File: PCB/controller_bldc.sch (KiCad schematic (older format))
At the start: 72 parts, among them J1 Battery Supply, J2 Conn_01x11_Male, J6 LM35, J7 Hall Sensors, J9 BLDC Motor, K1 RAYEX-L90B, Q1 IRF1010N, Q2 IRF1010N, Q3 IRF1010N, Q4 IRF1010N, Q5 IRF1010N, Q6 IRF1010N, Q7 PN2222A, U1 ESP32-DEVKITC-32D, U2 Opamp_Dual_Generic, U3 LM2596SOURCE_Pin2, U4 IR2103, U5 LM2596SOURCE, U8 IR2103, U9 IR2103

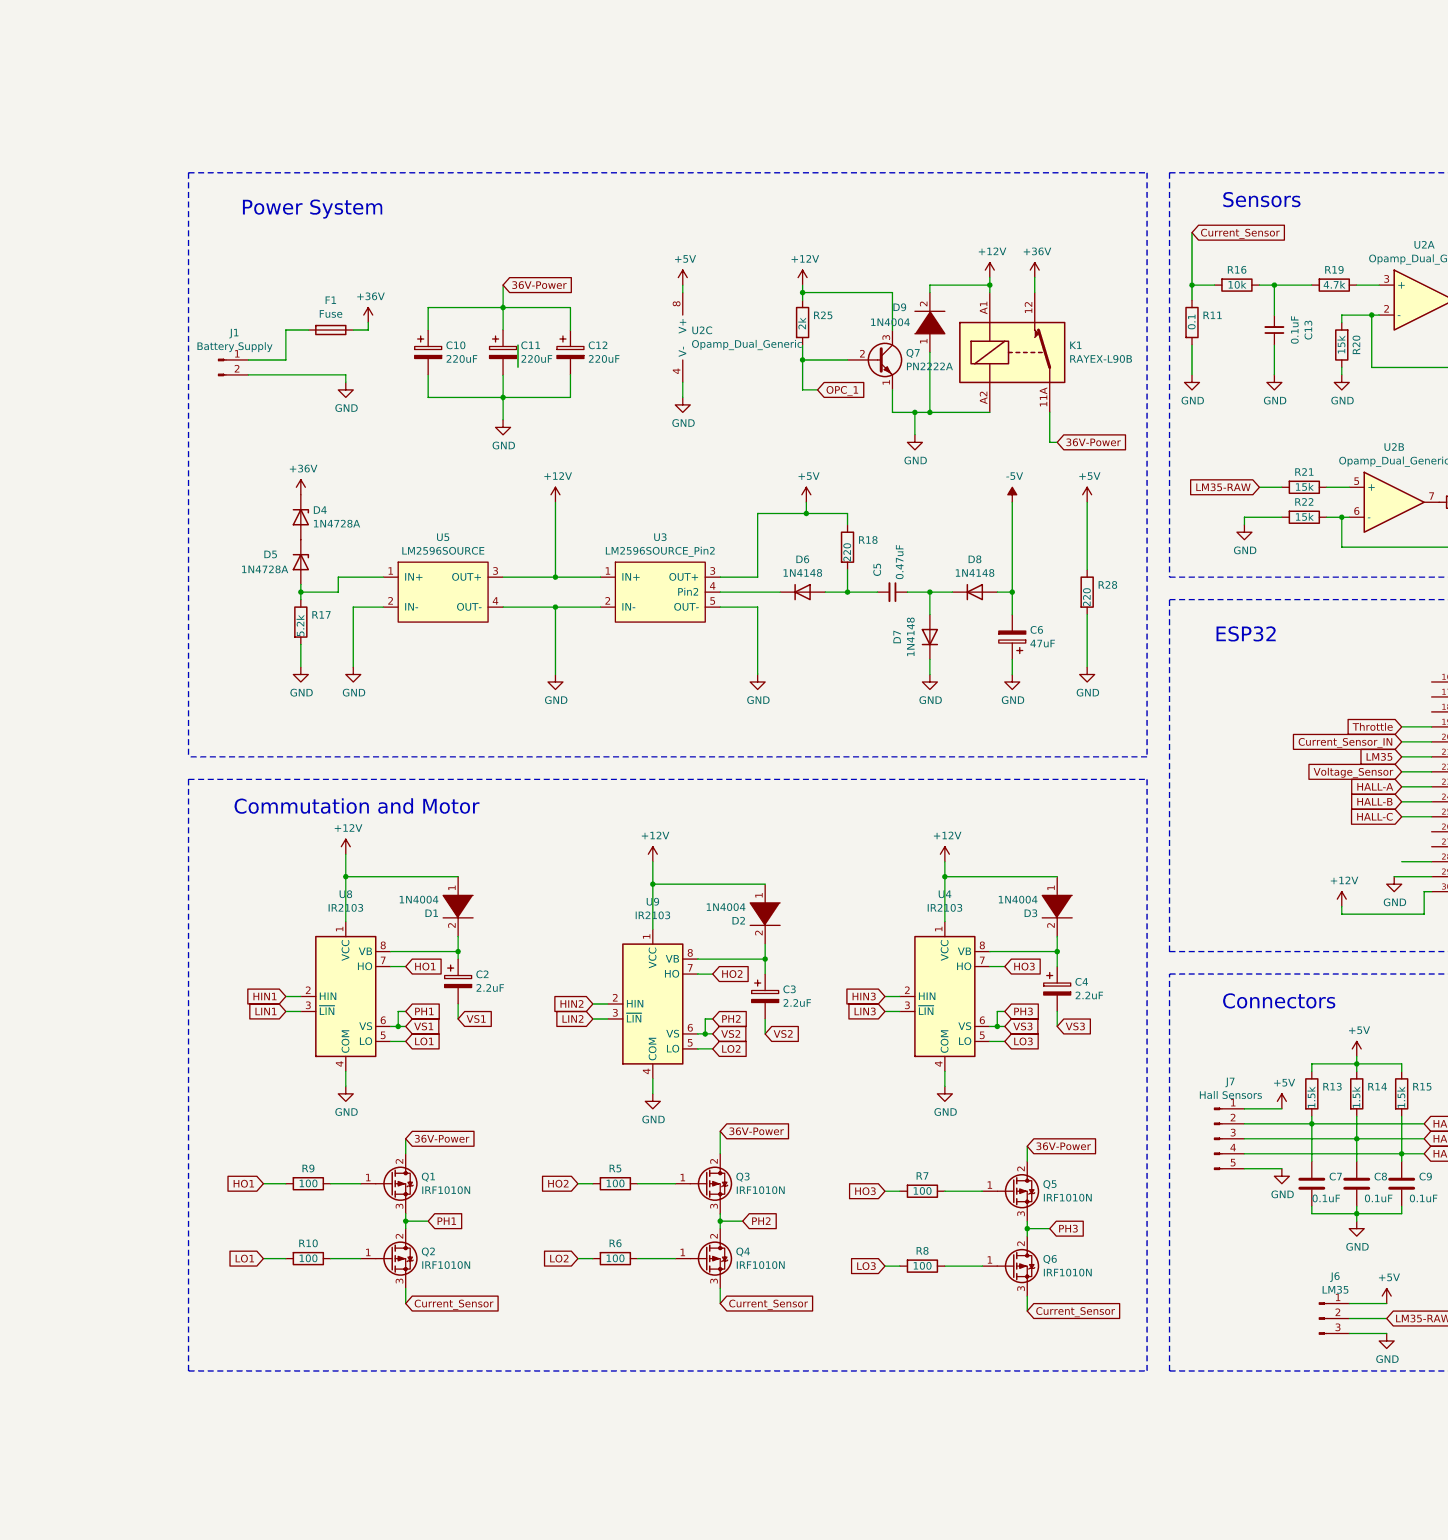
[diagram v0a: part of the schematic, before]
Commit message: Changing all the schematics
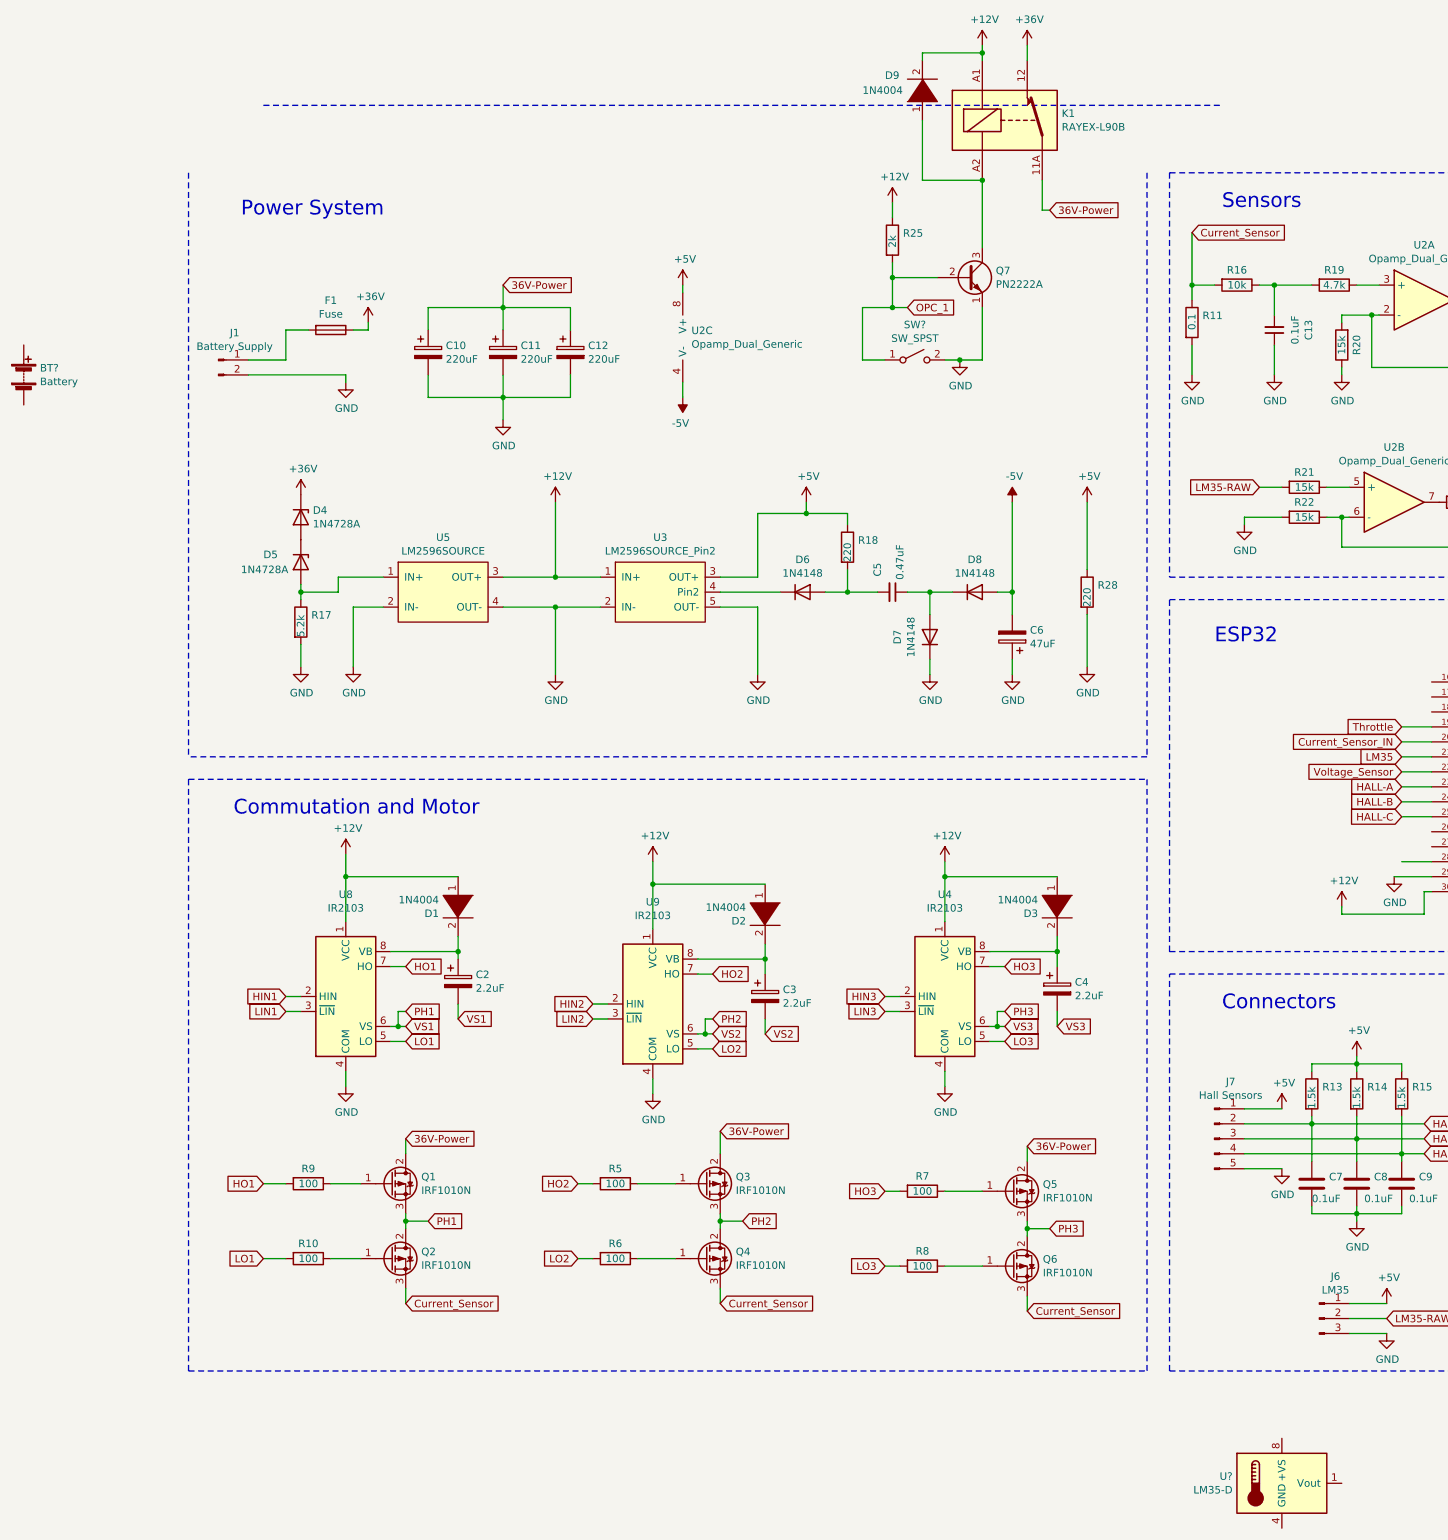
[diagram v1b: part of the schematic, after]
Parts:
- added BT?: Battery, symbol Device:Battery
- added SW?: SW_SPST, symbol Switch:SW_SPST
- added U?: LM35-D, Package_SO:SOIC-8_3.9x4.9mm_P1.27mm, symbol Sensor_Temperature:LM35-D
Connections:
- net +12V: no longer Q7.3 (C)
- net -5V: now also U2.4 (V-)
- net GND: now also SW?.2 (B); no longer D9.1 (K), K1.A2, U2.4 (V-)
- net OPC_1: now also SW?.1 (A)
- new net: D9.1 (K), K1.A2, Q7.3 (C)
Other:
- moved on the sheet: D9, K1, Q7, R25
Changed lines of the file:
@@
 	2700 1050 2250 1050
-Wire Wire Line
-	2350 1450 2350 1300
 Wire Wire Line
 	2250 1050 2250 1200
@@
 $EndComp
 Wire Wire Line
-	4250 1400 4550 1400
-Wire Wire Line
-	4250 1600 4250 1400
-Wire Wire Line
-	4350 1600 4250 1600
-Text GLabel 4350 1600 2    50   Input ~ 0
+	4850 850  5150 850
+Wire Wire Line
+	4850 1050 4850 850
+Wire Wire Line
+	4950 1050 4850 1050
+Text GLabel 4950 1050 2    50   Input ~ 0
 OPC_1
-Wire Wire Line
-	5000 1750 5100 1750
-Connection ~ 5000 1750
-Wire Wire Line
-	5000 1900 5000 1750
-Connection ~ 5100 1750
-Wire Wire Line
-	4850 1750 5000 1750
 $Comp
 L power:GND #PWR0109
 U 1 1 618C8BBA
-P 5000 1900
-F 0 "#PWR0109" H 5000 1650 50  0001 C CNN
-F 1 "GND" H 5005 1727 50  0000 C CNN
-F 2 "" H 5000 1900 50  0001 C CNN
-F 3 "" H 5000 1900 50  0001 C CNN
-	1    5000 1900
-	1    0    0    -1
-$EndComp
-Wire Wire Line
-	4850 1600 4850 1750
-Wire Wire Line
-	5100 1750 5500 1750
-Wire Wire Line
-	5100 1350 5100 1750
-Wire Wire Line
-	5500 900  5500 950
-Connection ~ 5500 900
-Wire Wire Line
-	5100 900  5500 900
-Wire Wire Line
-	5100 950  5100 900
-Wire Wire Line
-	4250 950  4850 950
-Wire Wire Line
-	4850 1200 4850 950
-Wire Wire Line
-	5500 850  5500 900
-Connection ~ 4250 950
-Wire Wire Line
-	4250 950  4250 1000
-Wire Wire Line
-	4250 900  4250 950
+P 5300 1400
+F 0 "#PWR0109" H 5300 1150 50  0001 C CNN
+F 1 "GND" H 5305 1227 50  0000 C CNN
+F 2 "" H 5300 1400 50  0001 C CNN
+F 3 "" H 5300 1400 50  0001 C CNN
+	1    5300 1400
+	1    0    0    -1
+$EndComp
+Wire Wire Line
+	5050 200  5450 200
+Wire Wire Line
+	5050 -200 5050 200
+Wire Wire Line
+	5450 -650 5450 -600
+Connection ~ 5450 -650
+Wire Wire Line
+	5050 -650 5450 -650
+Wire Wire Line
+	5050 -600 5050 -650
+Wire Wire Line
+	5450 -700 5450 -650
 $Comp
 L pspice:DIODE D9
 U 1 1 6101C203
-P 5100 1150
-F 0 "D9" V 5200 1400 50  0000 R CNN
-F 1 "1N4004" V 5100 1550 50  0000 R CNN
-F 2 "Diode_THT:D_DO-35_SOD27_P7.62mm_Horizontal" H 5100 1150 50  0001 C CNN
-F 3 "~" H 5100 1150 50  0001 C CNN
-	1    5100 1150
+P 5050 -400
+F 0 "D9" V 5150 -150 50  0000 R CNN
+F 1 "1N4004" V 5050 0   50  0000 R CNN
+F 2 "Diode_THT:D_DO-35_SOD27_P7.62mm_Horizontal" H 5050 -400 50  0001 C CNN
+F 3 "~" H 5050 -400 50  0001 C CNN
+	1    5050 -400
 	0    -1   -1   0
 $EndComp
 Wire Wire Line
-	5800 850  5800 950
+	5750 -700 5750 -600
 $Comp
 L Relay:RAYEX-L90B K1
 U 1 1 6114BA59
-P 5700 1350
-F 0 "K1" H 6030 1396 50  0000 L CNN
-F 1 "RAYEX-L90B" H 6030 1305 50  0000 L CNN
-F 2 "Relay_THT:Relay_SPST_RAYEX-L90B" H 6050 1300 50  0001 L CNN
-F 3 "https://a3.sofastcdn.com/attachment/7jioKBjnRiiSrjrjknRiwS77gwbf3zmp/L90-SERIES.pdf" H 6200 1200 50  0001 L CNN
-	1    5700 1350
+P 5650 -200
+F 0 "K1" H 5980 -154 50  0000 L CNN
+F 1 "RAYEX-L90B" H 5980 -245 50  0000 L CNN
+F 2 "Relay_THT:Relay_SPST_RAYEX-L90B" H 6000 -250 50  0001 L CNN
+F 3 "https://a3.sofastcdn.com/attachment/7jioKBjnRiiSrjrjknRiwS77gwbf3zmp/L90-SERIES.pdf" H 6150 -350 50  0001 L CNN
+	1    5650 -200
 	1    0    0    -1
 $EndComp
@@
 L Device:R R25
 U 1 1 61021042
-P 4250 1150
-F 0 "R25" H 4320 1196 50  0000 L CNN
-F 1 "2k" V 4250 1100 50  0000 L CNN
-F 2 "Resistor_THT:R_Axial_DIN0207_L6.3mm_D2.5mm_P10.16mm_Horizontal" V 4180 1150 50  0001 C CNN
-F 3 "~" H 4250 1150 50  0001 C CNN
-	1    4250 1150
+P 4850 600
+F 0 "R25" H 4920 646 50  0000 L CNN
+F 1 "2k" V 4850 550 50  0000 L CNN
+F 2 "Resistor_THT:R_Axial_DIN0207_L6.3mm_D2.5mm_P10.16mm_Horizontal" V 4780 600 50  0001 C CNN
+F 3 "~" H 4850 600 50  0001 C CNN
+	1    4850 600
 	1    0    0    -1
 $EndComp
@@
 L Transistor_BJT:PN2222A Q7
 U 1 1 6101E23D
-P 4750 1400
-F 0 "Q7" H 4940 1446 50  0000 L CNN
-F 1 "PN2222A" H 4940 1355 50  0000 L CNN
-F 2 "Package_TO_SOT_THT:TO-92_Inline" H 4950 1325 50  0001 L CIN
-F 3 "https://www.onsemi.com/pub/Collateral/PN2222-D.PDF" H 4750 1400 50  0001 L CNN
-	1    4750 1400
-	1    0    0    -1
-$EndComp
-Connection ~ 4250 1400
-Wire Wire Line
-	4250 1300 4250 1400
+P 5350 850
+F 0 "Q7" H 5540 896 50  0000 L CNN
+F 1 "PN2222A" H 5540 805 50  0000 L CNN
+F 2 "Package_TO_SOT_THT:TO-92_Inline" H 5550 775 50  0001 L CIN
+F 3 "https://www.onsemi.com/pub/Collateral/PN2222-D.PDF" H 5350 850 50  0001 L CNN
+	1    5350 850
+	1    0    0    -1
+$EndComp
+Connection ~ 4850 850
+Wire Wire Line
+	4850 750  4850 850
 $Comp
 L power:+12V #PWR0134
 U 1 1 6106A128
-P 5500 850
-F 0 "#PWR0134" H 5500 700 50  0001 C CNN
-F 1 "+12V" H 5515 1023 50  0000 C CNN
-F 2 "" H 5500 850 50  0001 C CNN
-F 3 "" H 5500 850 50  0001 C CNN
-	1    5500 850
-	1    0    0    -1
-$EndComp
-Wire Wire Line
-	5900 1750 5900 1950
+P 5450 -700
+F 0 "#PWR0134" H 5450 -850 50  0001 C CNN
+F 1 "+12V" H 5465 -527 50  0000 C CNN
+F 2 "" H 5450 -700 50  0001 C CNN
+F 3 "" H 5450 -700 50  0001 C CNN
+	1    5450 -700
+	1    0    0    -1
+$EndComp
+Wire Wire Line
+	5850 200  5850 400
 $Comp
 L power:+36V #PWR03
 U 1 1 607E0827
-P 5800 850
-F 0 "#PWR03" H 5800 700 50  0001 C CNN
-F 1 "+36V" H 5815 1023 50  0000 C CNN
-F 2 "" H 5800 850 50  0001 C CNN
-F 3 "" H 5800 850 50  0001 C CNN
-	1    5800 850
+P 5750 -700
+F 0 "#PWR03" H 5750 -850 50  0001 C CNN
+F 1 "+36V" H 5765 -527 50  0000 C CNN
+F 2 "" H 5750 -700 50  0001 C CNN
+F 3 "" H 5750 -700 50  0001 C CNN
+	1    5750 -700
 	1    0    0    -1
 $EndComp
@@
 L power:+12V #PWR0110
 U 1 1 60E85274
-P 4250 900
-F 0 "#PWR0110" H 4250 750 50  0001 C CNN
-F 1 "+12V" H 4265 1073 50  0000 C CNN
-F 2 "" H 4250 900 50  0001 C CNN
-F 3 "" H 4250 900 50  0001 C CNN
-	1    4250 900
-	1    0    0    -1
-$EndComp
-Wire Wire Line
-	5900 1950 5950 1950
-Text GLabel 5950 1950 2    50   Input ~ 0
+P 4850 350
+F 0 "#PWR0110" H 4850 200 50  0001 C CNN
+F 1 "+12V" H 4865 523 50  0000 C CNN
+F 2 "" H 4850 350 50  0001 C CNN
+F 3 "" H 4850 350 50  0001 C CNN
+	1    4850 350
+	1    0    0    -1
+$EndComp
+Wire Wire Line
+	5850 400  5900 400
+Text GLabel 5900 400  2    50   Input ~ 0
 36V-Power
 $Comp
@@
 Wire Wire Line
 	3450 1550 3450 1650
-$Comp
-L power:GND #PWR0131
-U 1 1 60CCCE5C
-P 3450 1650
-F 0 "#PWR0131" H 3450 1400 50  0001 C CNN
-F 1 "GND" H 3455 1477 50  0000 C CNN
-F 2 "" H 3450 1650 50  0001 C CNN
-F 3 "" H 3450 1650 50  0001 C CNN
-	1    3450 1650
-	1    0    0    -1
-$EndComp
 $Comp
 L power:+5V #PWR0130
@@
 LM35
 Wire Notes Line
-	150  150  6550 150
+	650  -300 7050 -300
 Wire Wire Line
 	800  1200 800  1400
@@
 Wire Wire Line
 	6150 2800 6150 2350
+$Comp
+L power:-5V #PWR0127
+U 1 1 609F2616
+P 3450 1650
+F 0 "#PWR0127" H 3450 1750 50  0001 C CNN
+F 1 "-5V" H 3465 1823 50  0000 C CNN
+F 2 "" H 3450 1650 50  0001 C CNN
+F 3 "" H 3450 1650 50  0001 C CNN
+	1    3450 1650
+	-1   0    0    1
+$EndComp
+$Comp
+L Switch:SW_SPST SW?
+U 1 1 60A2738A
+P 5000 1400
+F 0 "SW?" H 5000 1635 50  0000 C CNN
+F 1 "SW_SPST" H 5000 1544 50  0000 C CNN
+F 2 "" H 5000 1400 50  0001 C CNN
+F 3 "~" H 5000 1400 50  0001 C CNN
+	1    5000 1400
+	1    0    0    -1
+$EndComp
+Wire Wire Line
+	4800 1400 4650 1400
+Wire Wire Line
+	4650 1400 4650 1050
+Wire Wire Line
+	4650 1050 4850 1050
+Connection ~ 4850 1050
+Wire Wire Line
+	5200 1400 5300 1400
+$Comp
+L Device:Battery BT?
+U 1 1 60A5358C
+P -950 1500
+F 0 "BT?" H -842 1546 50  0000 L CNN
+F 1 "Battery" H -842 1455 50  0000 L CNN
+F 2 "" V -950 1560 50  0001 C CNN
+F 3 "~" V -950 1560 50  0001 C CNN
+	1    -950 1500
+	1    0    0    -1
+$EndComp
+$Comp
+L Sensor_Temperature:LM35-D U?
+U 1 1 60A5764A
+P 7450 8900
+F 0 "U?" H 7121 8946 50  0000 R CNN
+F 1 "LM35-D" H 7121 8855 50  0000 R CNN
+F 2 "Package_SO:SOIC-8_3.9x4.9mm_P1.27mm" H 7450 8500 50  0001 C CNN
+F 3 "http://www.ti.com/lit/ds/symlink/lm35.pdf" H 7450 8900 50  0001 C CNN
+	1    7450 8900
+	1    0    0    -1
+$EndComp
+Wire Wire Line
+	5450 1050 5450 1400
+Wire Wire Line
+	4850 350  4850 450
+Connection ~ 5300 1400
+Wire Wire Line
+	5300 1400 5450 1400
+Wire Wire Line
+	5450 200  5450 650
+Connection ~ 5450 200
 $EndSCHEMATC

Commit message: Just before separating folders and branches According to version independence
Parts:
- removed BT?: Battery, symbol Device:Battery
- removed D9: 1N4004, Diode_THT:D_DO-35_SOD27_P7.62mm_Horizontal, symbol pspice:DIODE
- removed K1: RAYEX-L90B, Relay_THT:Relay_SPST_RAYEX-L90B, symbol Relay:RAYEX-L90B
- removed Q7: PN2222A, Package_TO_SOT_THT:TO-92_Inline, symbol Transistor_BJT:PN2222A
- removed R25: 2k, Resistor_THT:R_Axial_DIN0207_L6.3mm_D2.5mm_P10.16mm_Horizontal, symbol Device:R
- removed SW?: SW_SPST, symbol Switch:SW_SPST
- removed U1: ESP32-DEVKITC-32D, ESP32-DEVKITC-32D_Electeam:MODULE_ESP32-DEVKITC-32D, symbol controller_bldc-rescue:ESP32-DEVKITC-32D-ESP32-DEVKITC-32D
- removed U3: LM2596SOURCE_Pin2, Package_TO_SOT_THT_Electeam:LM2596DCSourcePin2_Electeam, symbol Converter_DCDC_Electeam:LM2596SOURCE_Pin2
- removed U5: LM2596SOURCE, Package_TO_SOT_THT_Electeam:LM2596DCSource_Electeam, symbol Converter_DCDC_Electeam:LM2596SOURCE
- removed U?: LM35-D, Package_SO:SOIC-8_3.9x4.9mm_P1.27mm, symbol Sensor_Temperature:LM35-D
- added Q5, Q6: 2N2222, Package_TO_SOT_THT:TO-39-3, symbol Transistor_BJT:2N2219
- added Q9: IRF1010N, Package_TO_SOT_THT_Electeam:TO-220-3_Horizontal_TabDown, symbol Transistor_FET:IRF740
- added R15: 4.7k, Resistor_THT:R_Axial_DIN0207_L6.3mm_D2.5mm_P10.16mm_Horizontal, symbol Device:R
- added R16, R18: 1.5k, Resistor_THT:R_Axial_DIN0207_L6.3mm_D2.5mm_P10.16mm_Horizontal, symbol Device:R
- added R24: 2k, Resistor_THT:R_Axial_DIN0207_L6.3mm_D2.5mm_P10.16mm_Horizontal, symbol Device:R
- added U5: ESP32-DEVKITC-32D, MODULE_ESP32-DEVKITC-32D, symbol ESP32-DEVKITC-32D:ESP32-DEVKITC-32D
- J1: value Battery Supply -> Battery after BMS Supply
- U4: renamed from U2; value Opamp_Dual_Generic -> AmpOp_Dual_Generic
- renumbered C2 to C1, C1 to C10, C7 to C11, C8 to C12, C9 to C13, C3 to C2, C5 to C3, C6 to C4, C4 to C5, C10 to C6, C11 to C7, C12 to C8, C13 to C9, D4 to D1, D5 to D2, D1 to D3, D2 to D4, D6 to D5, D7 to D6, D8 to D7, D3 to D8, J9 to J2, J7 to J3, J2 to J4, J6 to J5, Q5 to Q7, Q6 to Q8, R17 to R1, R21 to R10, R22 to R11, R19 to R12, R20 to R13, R29 to R14, R24 to R17, R23 to R19, R18 to R2, R7 to R20, R8 to R21, R26 to R22, R27 to R23, R3 to R25, R1 to R26, R2 to R27, R4 to R28, R13 to R29, R9 to R3, R14 to R30, R15 to R31, R12 to R32, R10 to R4, R11 to R5, R5 to R6, R6 to R7, R16 to R8, R28 to R9, U8 to U1, U9 to U2, U4 to U3
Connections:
- net +12V: now also R15.1, R24.1, U5.30 (EXT_5V)
- net +3V3: now also U5.1 (3V3)
- net 36V-Power: no longer C6.1, C7.1, C8.1
- net Brake: now also U5.10 (IO19)
- net Current_Sensor: now also Q9.2 (D); no longer R5.1, R8.2
- net Current_Sensor_IN: now also U5.20 (IO35)
- net GND: now also Q5.1 (E), Q6.1 (E), U5.2 (GND1), U5.29 (GND2)
- net HALL-A: now also U5.23 (IO25)
- net HALL-B: now also U5.24 (IO26)
- net HALL-C: now also U5.25 (IO27)
- net HIN1: now also U5.3 (IO15)
- net HIN2: now also U5.6 (IO16)
- net HIN3: now also U5.8 (IO5)
- net LIN1: now also U5.5 (IO4)
- net LIN2: now also U5.7 (IO17)
- net LIN3: now also U5.9 (IO18)
- net LM35: now also U5.21 (IO32)
- net OPC_1: now also R15.2, R16.2
- net RX-LCD: now also U5.13 (TXD0-IO1)
- net TX-LCD: now also U5.12 (RXD0-IO3)
- net Voltage_Sensor: now also U5.22 (IO33)
- net Throttle: no longer names the net of R14.2
- net Throttle: now also U5.19 (IO34)
- new net: Q6.2 (B), R18.2
- new net: Q5.2 (B), R16.1
- new net: Q5.3 (C), Q6.3 (C), Q9.1 (G), R24.2
- new net 36V-Motor: C6.1, C7.1, C8.1
- new net D-IRF1010N: Q9.3 (S), R5.1, R8.2
- new net HC-Control: R18.1
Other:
- note added: "Commutation"
- note added: "Energy System"
- note added: "High Current"
- note added: "Low Current"
- note added: "Motor\n"
- note removed: "Commutation and Motor\n"
- moved on the sheet: C1, C10, C11, C12, C13, C2, C3, C4, C5, C6, C7, C8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
